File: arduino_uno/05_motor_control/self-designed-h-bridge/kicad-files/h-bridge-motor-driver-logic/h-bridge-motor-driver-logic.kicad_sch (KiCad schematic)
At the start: 7 parts, among them J1 Conn_01x04_Pin, J2 Conn_01x04_Pin, U1 PC847

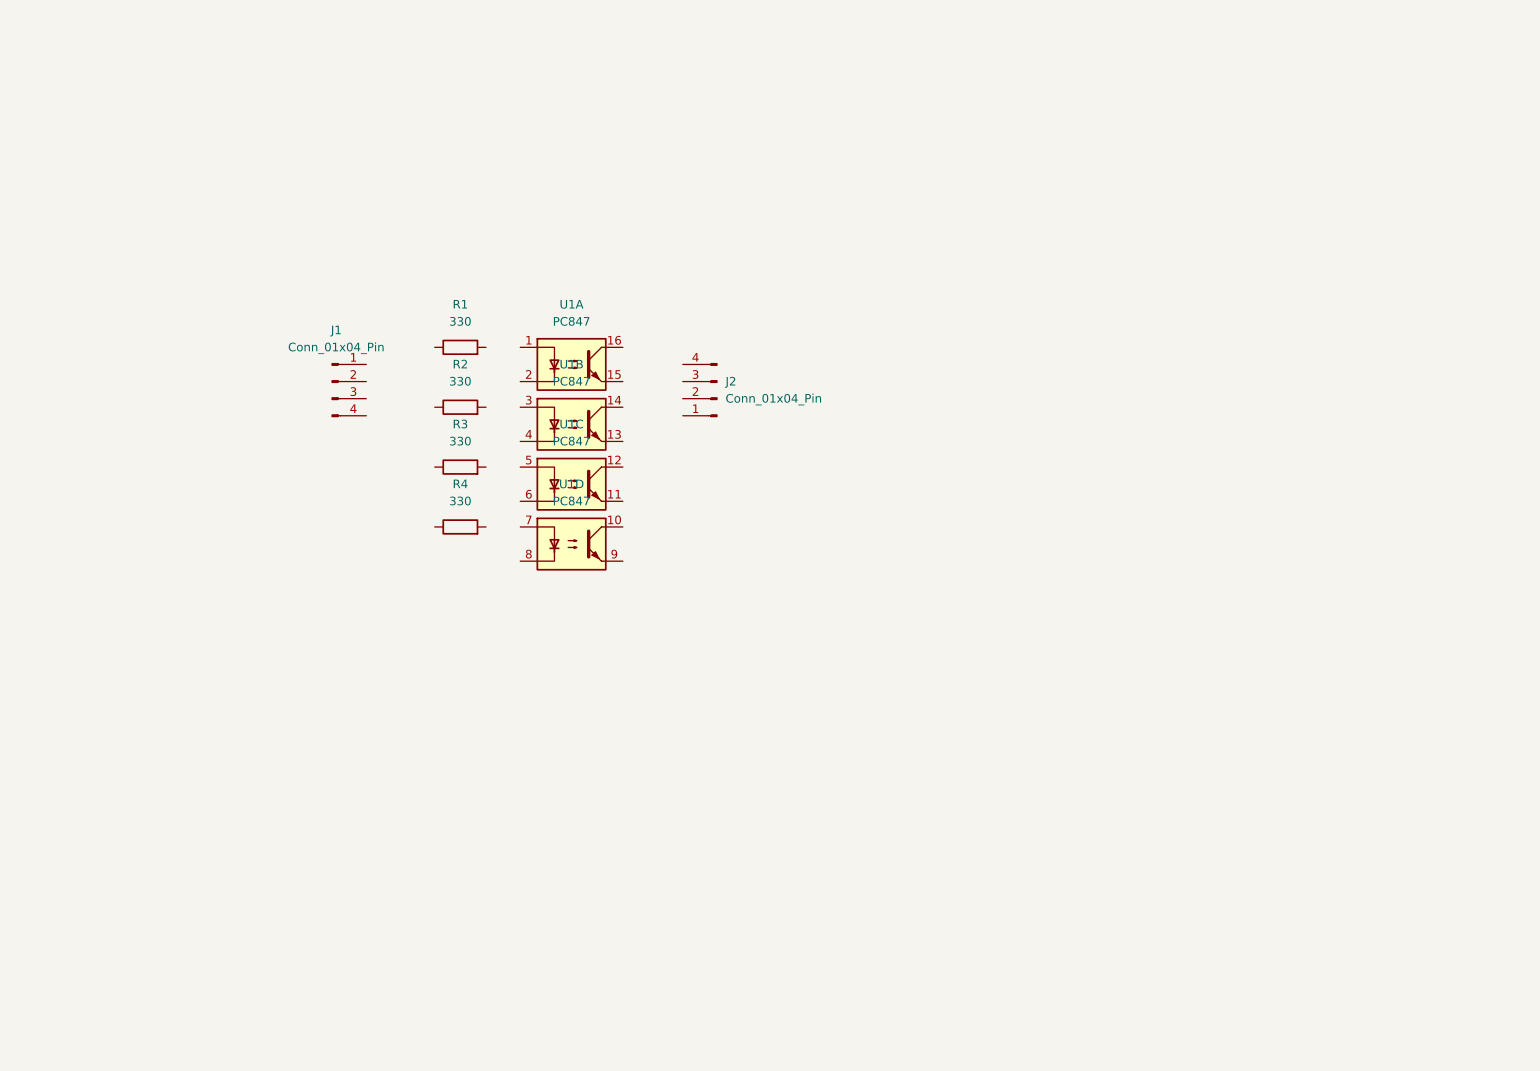
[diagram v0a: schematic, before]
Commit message: add labels to connector
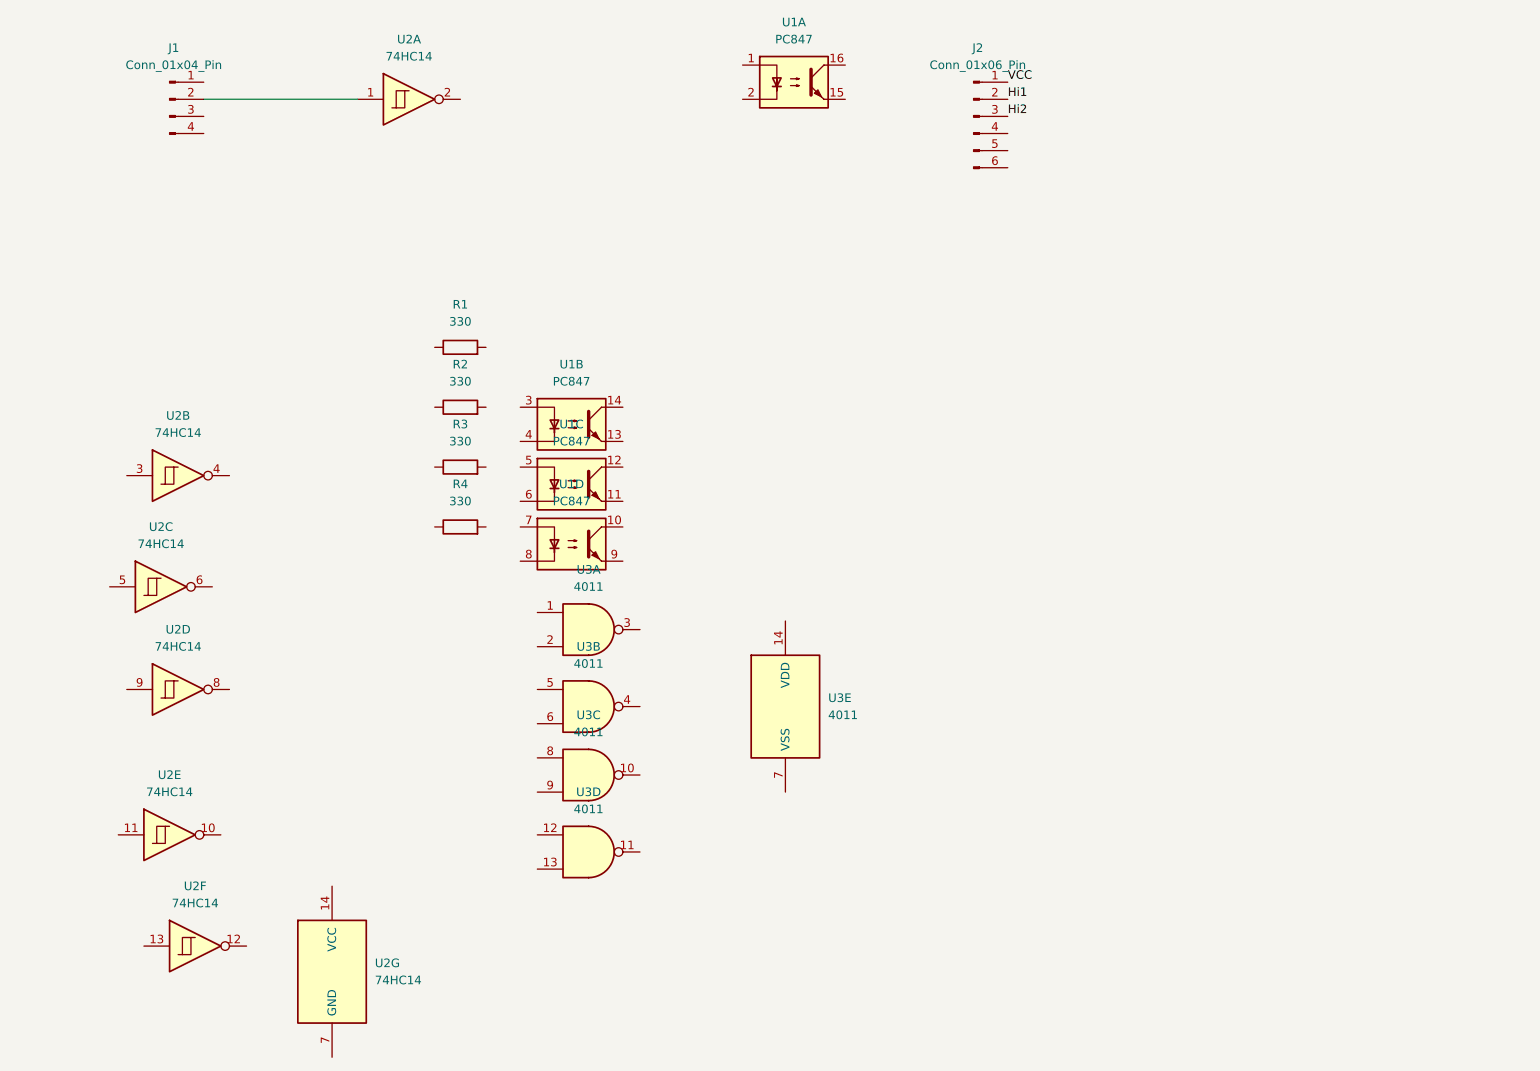
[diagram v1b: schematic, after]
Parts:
- removed J2: Conn_01x04_Pin, symbol Connector:Conn_01x04_Pin
- added J2: Conn_01x06_Pin, symbol Connector:Conn_01x06_Pin
- added U2: 74HC14, symbol 74xx:74HC14
- added U3: 4011, symbol 4xxx:4011
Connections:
- net at J1.2 (Pin_2): now also U2.1
- new net Hi1: J2.2 (Pin_2)
- new net Hi2: J2.3 (Pin_3)
- new net VCC: J2.1 (Pin_1)
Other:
- moved on the sheet: J1, U1A

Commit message: add wiring
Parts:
- removed J1: Conn_01x04_Pin, symbol Connector:Conn_01x04_Pin
- added J1: Conn_01x06_Pin, symbol Connector:Conn_01x06_Pin
- J2: value Conn_01x06_Pin -> H-Bridge Left
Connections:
- net Hi1: now also U1.15
- net Hi2: now also U1.13
- net VCC: now also U1.10, U1.12, U1.14, U1.16, J1.1 (Pin_1)
- net DIRL: now reaches R2.1
- net DIRL: now also U2.1, U3.5, J1.2 (Pin_2)
- net at R2.2: now also U1.3
- net at U1.7: now also R4.2
- net GND1: now reaches U1.8
- net GND1: now also U1.2, U1.4, U1.6
- net Lo2: now reaches U1.9
- net Lo2: now also J2.5 (Pin_5)
- net at R1.1: now also U2.2, U3.12
- net at R1.2: now also U1.1
- net at U3.11: now also U3.8, U3.9
- net PWML: now reaches U3.13
- net PWML: now also U3.6, J1.3 (Pin_3)
- net Lo1: now reaches J2.4 (Pin_4)
- net Lo1: now also U1.11
- net GND: now reaches J2.6 (Pin_6)
- net GND: now also J1.6 (Pin_6)
- net at U3.10: now also R4.1
- net at U3.1: now also U3.2, U3.4
- net at U3.3: now also R3.1
- net at U1.5: now also R3.2
- new net DIRR: J1.4 (Pin_4)
- new net PWMR: J1.5 (Pin_5)
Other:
- moved on the sheet: J2, R1, R2, R3, R4, U1A, U1B, U1C, U1D, U2G, U3A, U3B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

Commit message: add power flags / no connect
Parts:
- added C1, C2: 100nF, symbol Device:C
- R1, R2, R3, R4: footprint (none) -> Resistor_THT:R_Axial_DIN0207_L6.3mm_D2.5mm_P10.16mm_Horizontal
- U2, U3: footprint (none) -> Package_DIP:DIP-14_W7.62mm
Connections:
- net GND: no longer J1.6 (Pin_6)
- net GND1: now also J1.6 (Pin_6), U2.11, U2.13, U2.3, U2.5, U2.7 (GND), U2.9, U3.7 (VSS), C1.2, C2.2
- net VCC: now also U2.14 (VCC), U3.14 (VDD), C1.1, C2.1
- no-connect marks 0 -> 8
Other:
- moved on the sheet: U2B, U2C, U2D, U2E, U2F, U3E
